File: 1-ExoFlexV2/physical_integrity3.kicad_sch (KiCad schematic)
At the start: 35 parts, among them J88 100k, J89 100k, J90 100k, J91 100k, J92 100k, J93 100k, J94 100k, U82 SN74LVC1G32DBVR, U83 SN74LVC1G32DBVR, U84 SN74LVC1G32DBVR, U94 SN74LVC1G32DBVR, U95 SN74LVC1G32DBVR, U96 SN74LVC1G32DBVR

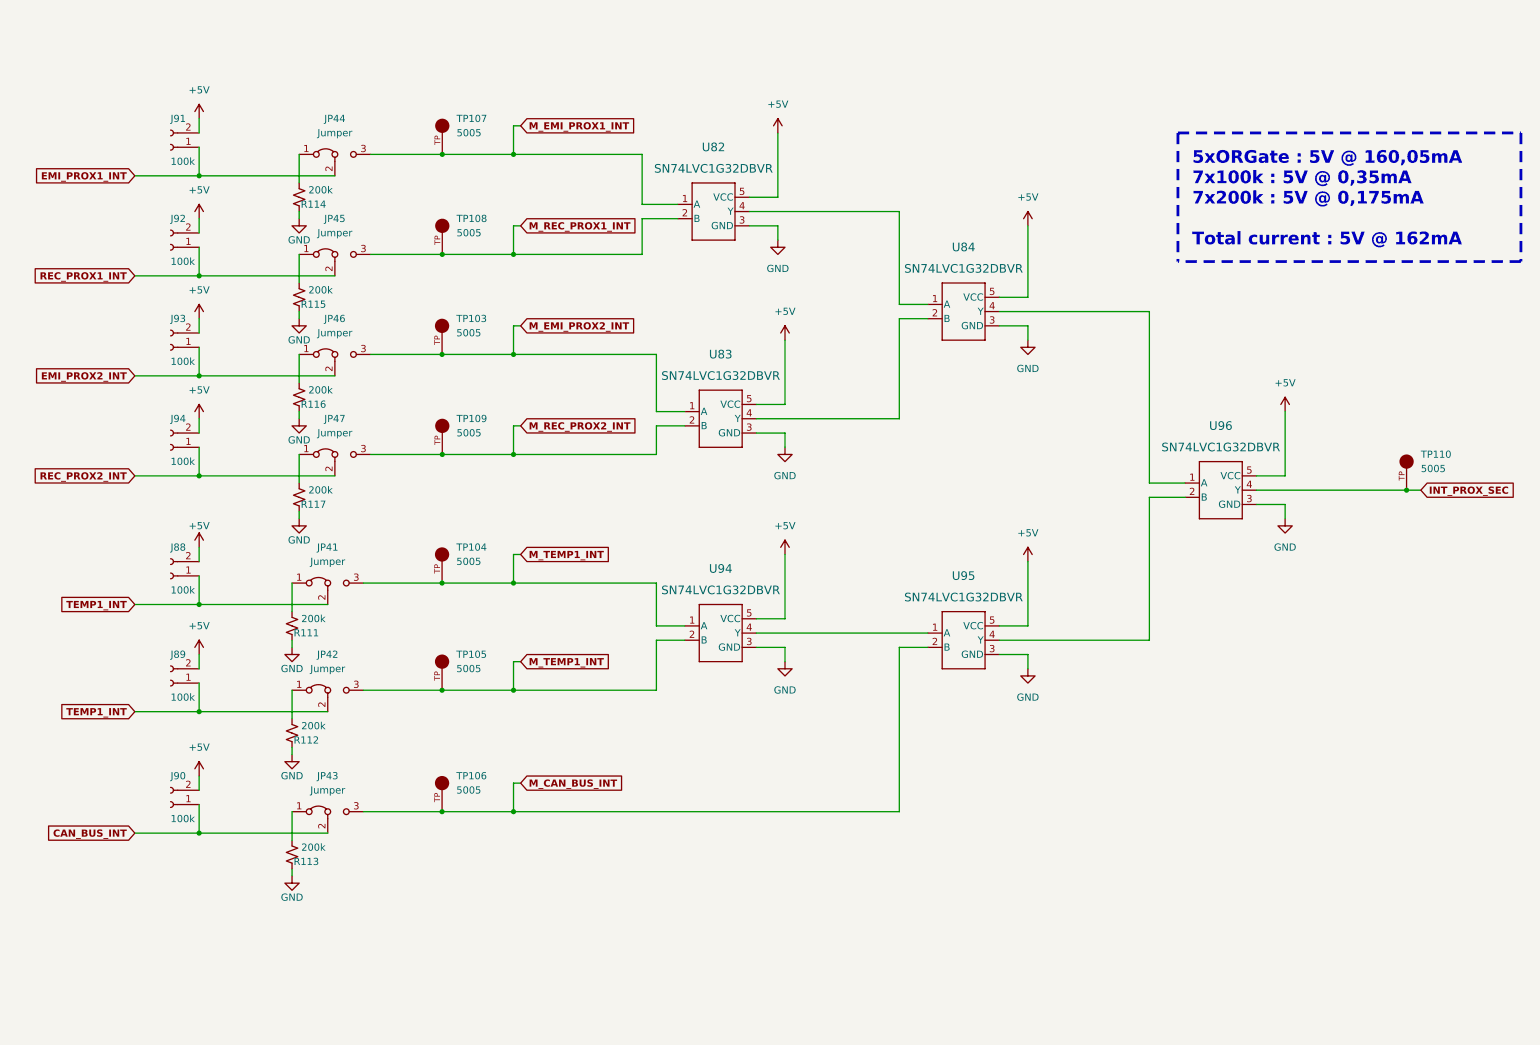
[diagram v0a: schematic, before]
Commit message: Chokes et RC
- Ajout des RF chokes
- Changement des résistance pour 0805
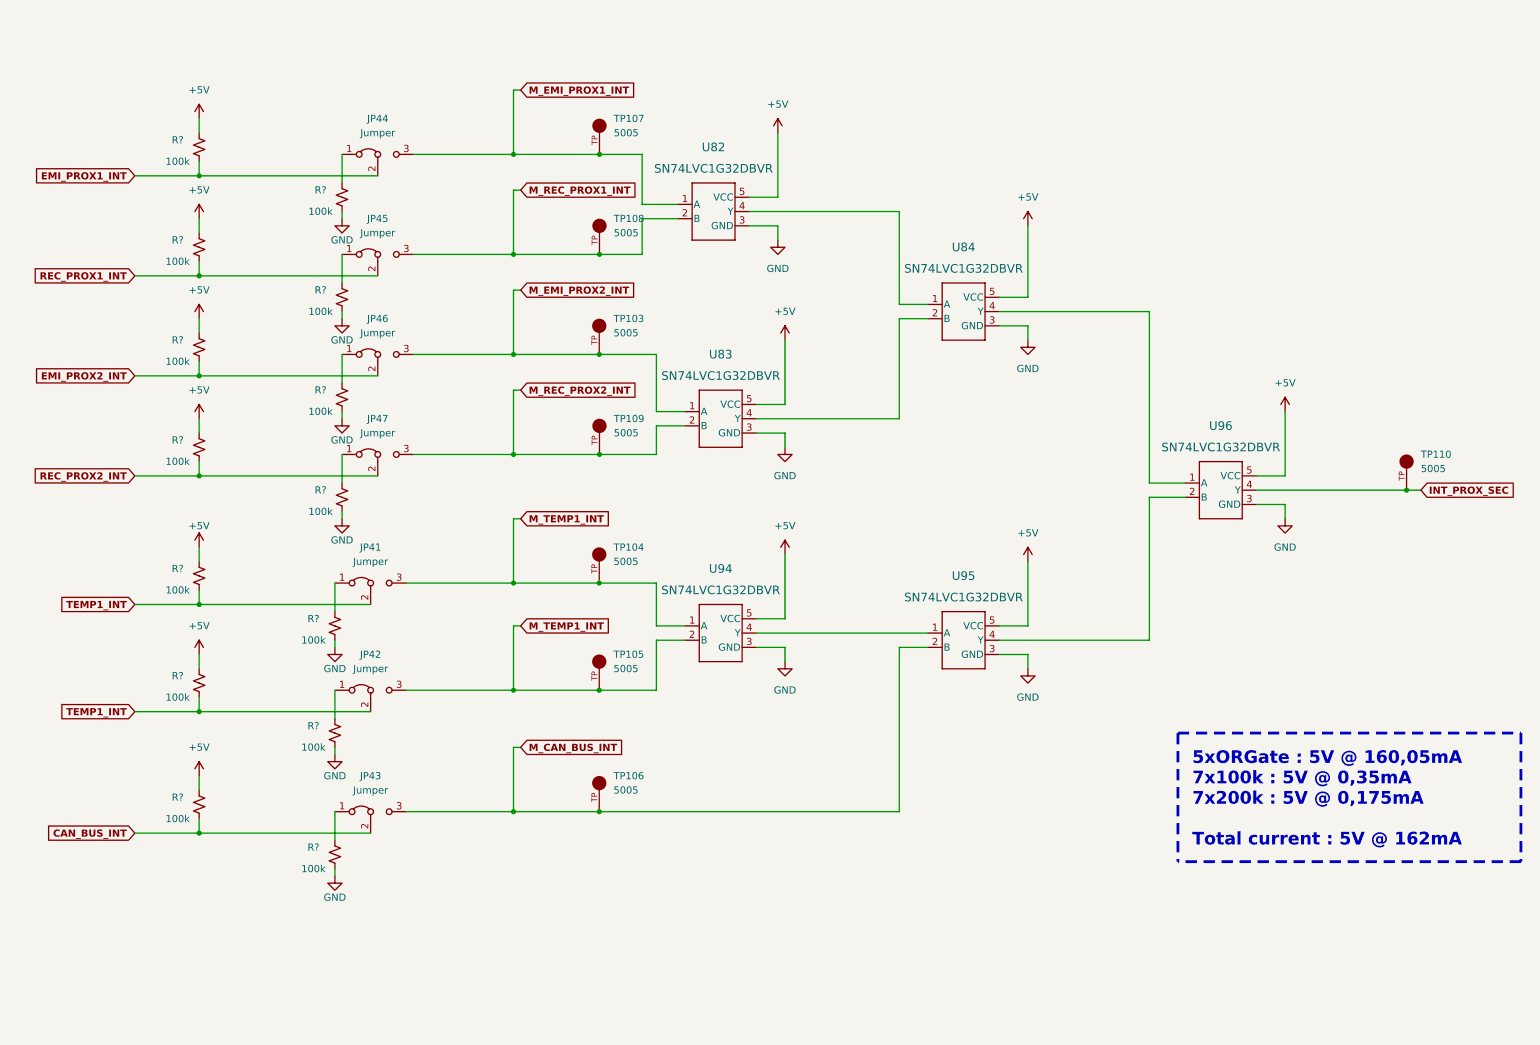
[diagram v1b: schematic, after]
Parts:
- removed J88, J89, J90, J91, J92, J93, J94: 100k, Connector_PinHeader_2.54mm:PinHeader_1x02_P2.54mm_Vertical, symbol Connector:Conn_01x02_Female
- removed R111, R112, R113, R114, R115, R116, R117: 200k, Resistor_SMD:R_0603_1608Metric, symbol Device:R_Small_US
- added R? (x14): 100k, Resistor_SMD:R_0805_2012Metric, symbol Device:R_Small_US
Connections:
- net +5V: now also R?.1, R?.1, R?.1, R?.1, R?.1, R?.1, R?.1
- net CAN_BUS_INT: now also R?.2
- net EMI_PROX1_INT: now also R?.2
- net EMI_PROX2_INT: now also R?.2
- net GND: now also R?.2, R?.2, R?.2, R?.2, R?.2, R?.2, R?.2
- net REC_PROX1_INT: now also R?.2
- net REC_PROX2_INT: now also R?.2
- net TEMP1_INT: now also R?.2, R?.2
- net at JP45.1 (A): now also R?.1
- net at JP41.1 (A): now also R?.1
- net at JP44.1 (A): now also R?.1
- net at JP46.1 (A): now also R?.1
- net at JP47.1 (A): now also R?.1
- net at JP43.1 (A): now also R?.1
- net at JP42.1 (A): now also R?.1
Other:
- moved on the sheet: JP41, JP42, JP43, JP44, JP45, JP46, JP47, TP103, TP104, TP105, TP106, TP107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

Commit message: Trimmer et jumper
-Changement de symbole de jumper
-Ajout des des trimmer aux endroits nécessaires
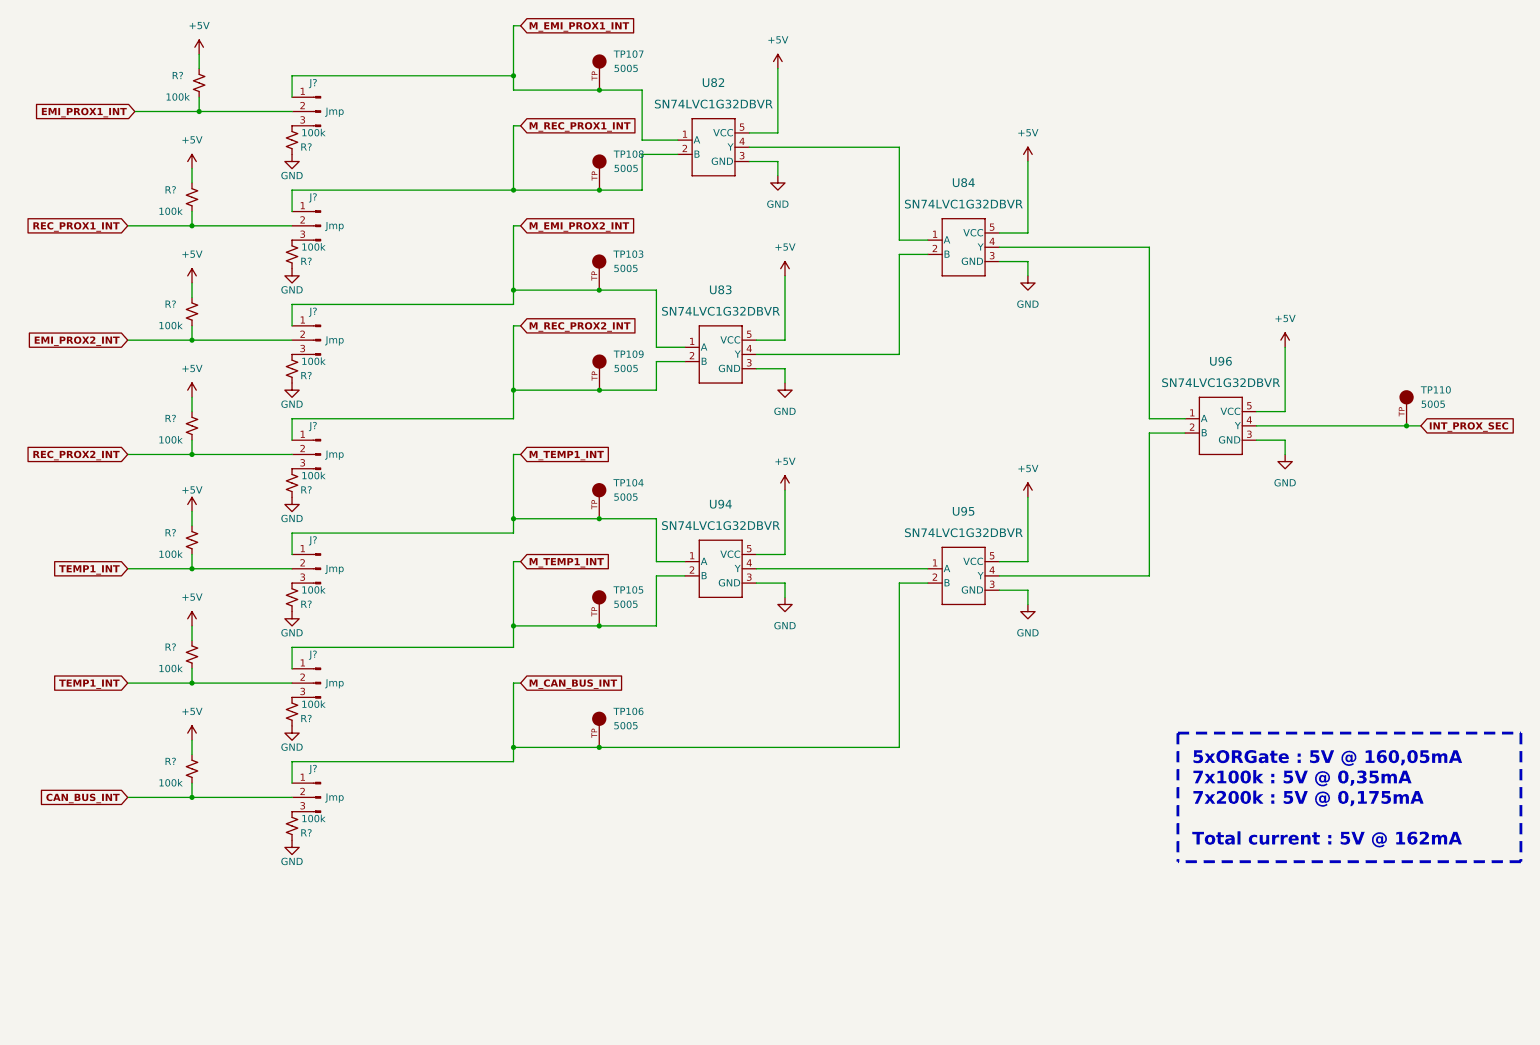
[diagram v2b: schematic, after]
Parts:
- removed JP41, JP42, JP43, JP44, JP45, JP46, JP47: Jumper, Connector_PinHeader_2.54mm:PinHeader_1x03_P2.54mm_Vertical, symbol Jumper:Jumper_3_Bridged12
- removed R? (x7): 100k, Resistor_SMD:R_0805_2012Metric, symbol Device:R_Small_US
- added J? (x7): Jmp, symbol Connector:Conn_01x03_Male
- added R? (x7): 100k, Resistor_SMD:R_0805_2012Metric, symbol Device:R_Small_US
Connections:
- net CAN_BUS_INT: now also J?.2 (Pin_2)
- net EMI_PROX1_INT: now also J?.2 (Pin_2)
- net EMI_PROX2_INT: now also J?.2 (Pin_2)
- net GND: now also R?.2, R?.2, R?.2, R?.2, R?.2, R?.2, R?.2
- net M_CAN_BUS_INT: now also J?.1 (Pin_1)
- net M_EMI_PROX1_INT: now also J?.1 (Pin_1)
- net M_EMI_PROX2_INT: now also J?.1 (Pin_1)
- net M_REC_PROX1_INT: now also J?.1 (Pin_1)
- net M_REC_PROX2_INT: now also J?.1 (Pin_1)
- net M_TEMP1_INT: now also J?.1 (Pin_1), J?.1 (Pin_1)
- net REC_PROX1_INT: now also J?.2 (Pin_2)
- net REC_PROX2_INT: now also J?.2 (Pin_2)
- net TEMP1_INT: now also J?.2 (Pin_2), J?.2 (Pin_2)
- new net: J?.3 (Pin_3), R?.1 (x7)
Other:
- moved on the sheet: R?, TP103, TP104, TP105, TP106, TP107, TP108, TP109, TP110, U82, U83, U84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

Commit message: Test points et notes
- Ajout de tous les tests point nécessaires
-  Ajoute des sections de notes dans chaque page
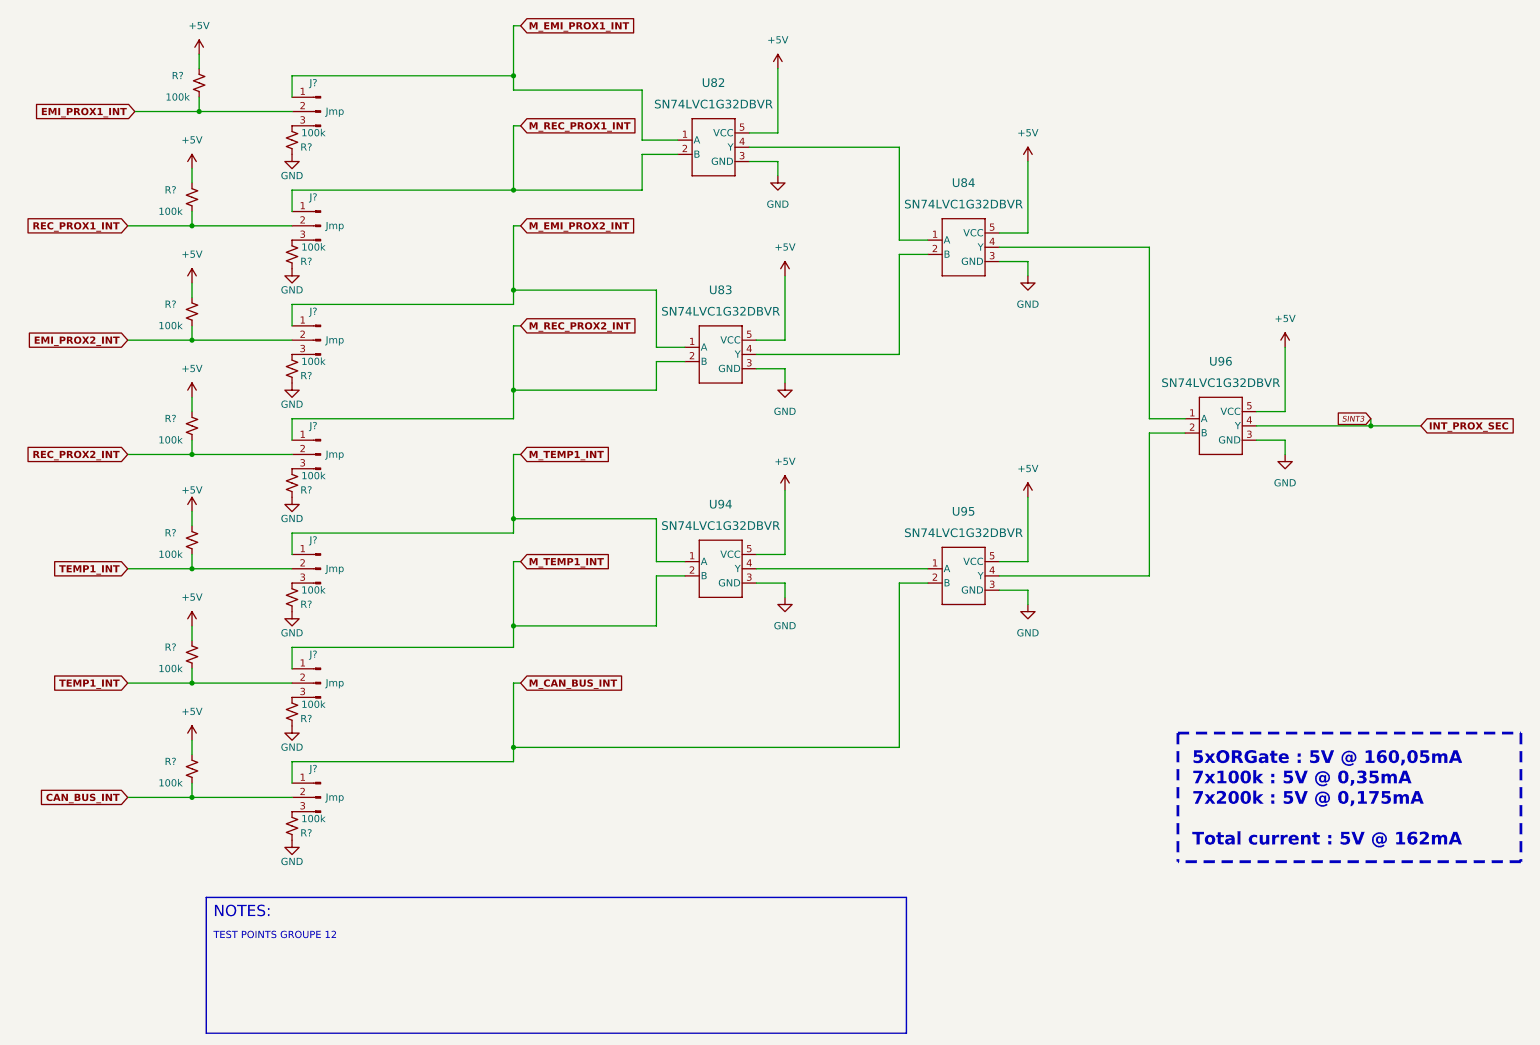
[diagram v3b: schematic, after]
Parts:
- removed TP103, TP104, TP105, TP106, TP107, TP108, TP109, TP110: 5005, FootPrint:KEYSTONE_5005, symbol SymLib:5005
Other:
- note added: "NOTES:"
- note added: "TEST POINTS GROUPE 12"

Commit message: Schématisation terminée
- Schéma terminé
- Passage vers le PCB
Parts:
- J123, J124, J125, J126, J127, J128, J129: renamed from J?; value Jmp -> Jumper; footprint (none) -> Connector_PinSocket_2.54mm:PinSocket_1x03_P2.54mm_Vertical; DESCRIPTION (none) -> CONN HEADER VERT 3POS 2.54MM; MANUFACTURER (none) -> Würth Elektronik; PACKAGE (none) -> Square 0.100" (2.54mm); PART NUMBER (none) -> 61300311121; TYPE (none) -> Through Hole
- R194, R195, R196, R197, R198, R199, R200, R201, R202, R203, R204, R205, R206, R207: renamed from R?; value 100k -> 100k 5% 1/8W; DESCRIPTION (none) -> 100 kOhms ±5% 0.125W, 1/8W Chip Resistor 0805 (2012 Metric)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; MANUFACTURER (none) -> Panasonic Electronic Components; PACKAGE (none) -> 0805 (2012 Metric); PART NUMBER (none) -> ERJ-6GEYJ104V; TYPE (none) -> SMD
- U100: renamed from U94; value SN74LVC1G32DBVR -> OR Gate; DESCRIPTION (none) -> OR Gate IC 1 Channel SOT-23-5; MANUFACTURER (none) -> Texas Instruments; PACKAGE (none) -> SC-74A, SOT-753; PART NUMBER (none) -> SN74LVC1G32DBVR; TYPE (none) -> SMD
- U101: renamed from U84; value SN74LVC1G32DBVR -> OR Gate; DESCRIPTION (none) -> OR Gate IC 1 Channel SOT-23-5; MANUFACTURER (none) -> Texas Instruments; PACKAGE (none) -> SC-74A, SOT-753; PART NUMBER (none) -> SN74LVC1G32DBVR; TYPE (none) -> SMD
- U102: renamed from U95; value SN74LVC1G32DBVR -> OR Gate; DESCRIPTION (none) -> OR Gate IC 1 Channel SOT-23-5; MANUFACTURER (none) -> Texas Instruments; PACKAGE (none) -> SC-74A, SOT-753; PART NUMBER (none) -> SN74LVC1G32DBVR; TYPE (none) -> SMD
- U103: renamed from U96; value SN74LVC1G32DBVR -> OR Gate; DESCRIPTION (none) -> OR Gate IC 1 Channel SOT-23-5; MANUFACTURER (none) -> Texas Instruments; PACKAGE (none) -> SC-74A, SOT-753; PART NUMBER (none) -> SN74LVC1G32DBVR; TYPE (none) -> SMD
- U98: renamed from U82; value SN74LVC1G32DBVR -> OR Gate; DESCRIPTION (none) -> OR Gate IC 1 Channel SOT-23-5; MANUFACTURER (none) -> Texas Instruments; PACKAGE (none) -> SC-74A, SOT-753; PART NUMBER (none) -> SN74LVC1G32DBVR; TYPE (none) -> SMD
- U99: renamed from U83; value SN74LVC1G32DBVR -> OR Gate; DESCRIPTION (none) -> OR Gate IC 1 Channel SOT-23-5; MANUFACTURER (none) -> Texas Instruments; PACKAGE (none) -> SC-74A, SOT-753; PART NUMBER (none) -> SN74LVC1G32DBVR; TYPE (none) -> SMD
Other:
- note added: "6xORGate : 5V @ 192,06mA 14x100k : 5V @ 0,7mA Total current : 5V @ 197mA"
- note removed: "5xORGate : 5V @ 160,05mA 7x100k : 5V @ 0,35mA 7x200k : 5V @ 0,175mA Total current : 5V @ 162mA"
- moved on the sheet: R194, R195, R196, R197, R198, R199, R200
